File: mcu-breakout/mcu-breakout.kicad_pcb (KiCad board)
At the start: 2 copper layers, 47 x 59.5 mm, 21 parts, among them J1 SCALE 3, J2 SCALE 2, J3 SCALE 1, J4 Spare, J5 Environment, SW1 Mod, SW2 Reset

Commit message: initial version for production
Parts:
- added REF**: Mounting Hole, Chof747_BoardModifications:Mounting Hole, F.Cu at (78.0, 54.9)
- added REF**: Mounting Hole, Chof747_BoardModifications:Mounting Hole, F.Cu at (117.8, 107.2)
- J5: footprint Connector_JST:JST_XH_B4B-XH-A_1x04_P2.50mm_Vertical -> Chof747_Connectors:JST_XH_B4B-XH-A_1x04_P2.54mm_Vertical
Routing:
- net AREF: track 124.2 -> 119.6 mm
- net LED_2: track 97.9 -> 97.1 mm
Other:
- outline, holes or cut-outs redrawn
- board text added: "5V"
- board text removed: "VCC (5V)"

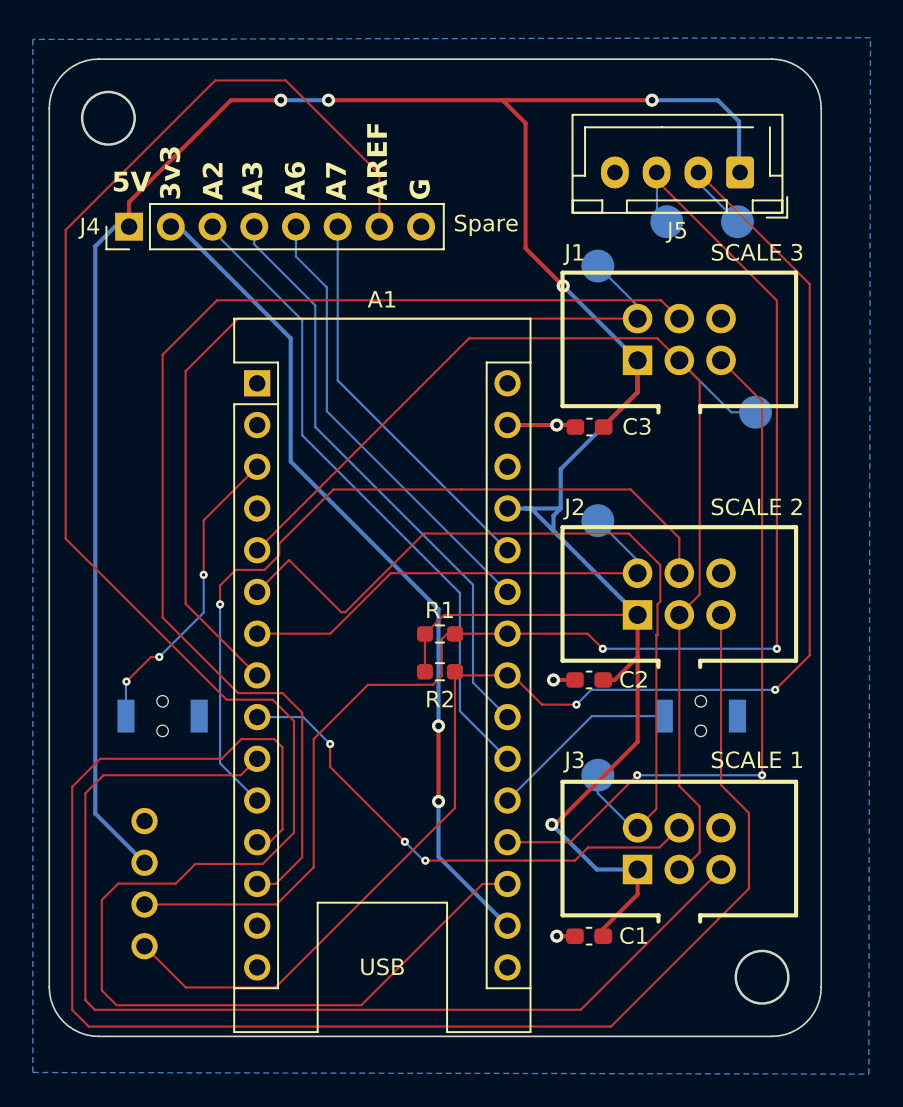
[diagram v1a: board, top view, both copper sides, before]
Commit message: Changed to separeted clock lines for the different scales
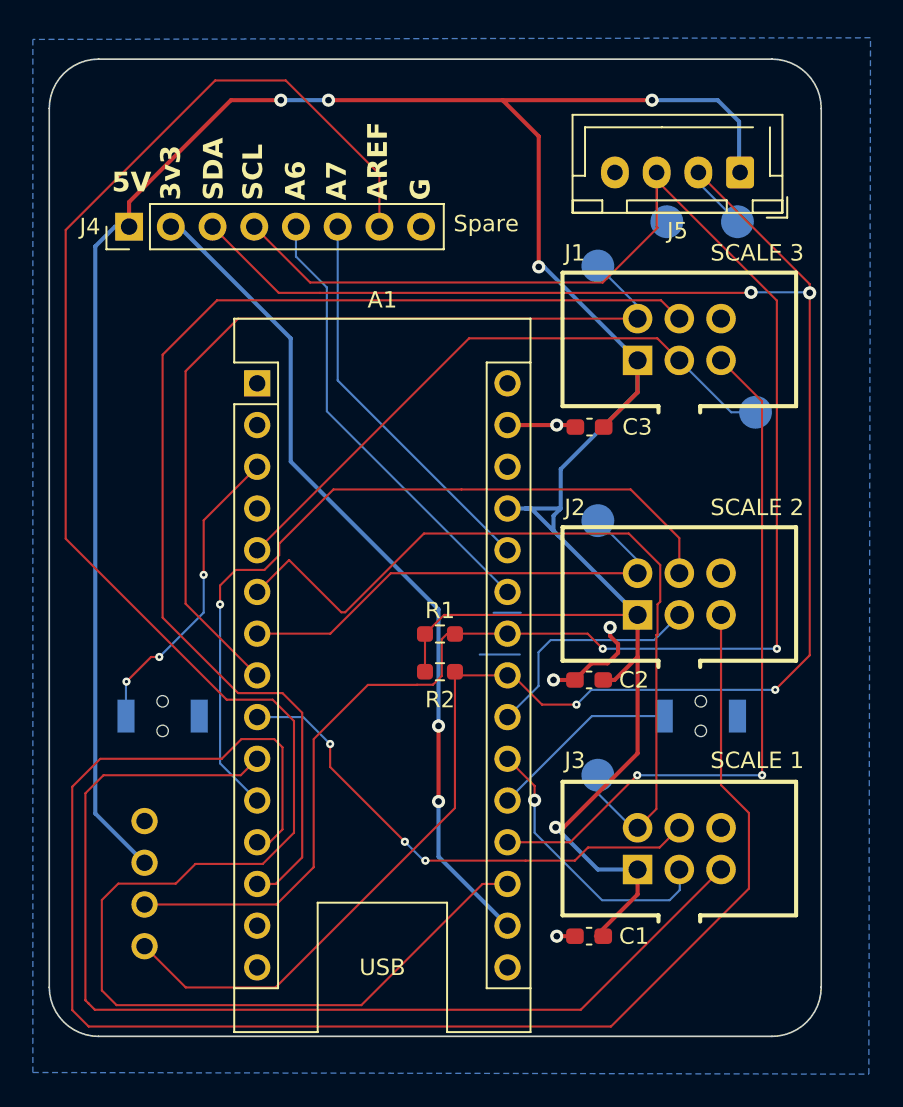
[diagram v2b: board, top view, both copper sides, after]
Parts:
- removed REF** (x2): Mounting Hole, Chof747_BoardModifications:Mounting Hole
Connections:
- A1 pad 21: A2 -> CLK_1
- A1 pad 22: A3 -> CLK_2
- A1 pad 5: CLK -> CLK_3
- J1 pad 3: CLK -> CLK_3
- J2 pad 3: CLK -> CLK_2
- J3 pad 3: CLK -> CLK_1
- J4 pad 3: A2 -> SDA
- J4 pad 4: A3 -> SCL
- TP4 pad 1: CLK -> CLK_3
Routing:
- net CLK: track 70.7 -> 0.00 mm
- net A2: track 39.8 -> 0.00 mm
- net SDA: track 92.6 -> 130.7 mm, vias 2 -> 4
- net CLK_3: track 0.00 -> 37.5 mm
- net A3: track 36.2 -> 0.00 mm
- net SCL: track 86.9 -> 117.6 mm
- net CLK_1: track 0.00 -> 17.2 mm, vias 0 -> 1
- net CLK_2: track 0.00 -> 14.2 mm
- net GND: track 6.59 -> 15.7 mm, vias 3 -> 4
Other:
- board text added: "Samla Filamentalist Controller Board v1.1 (c)2026 chof"
- board text removed: "A2"
- board text removed: "A3"
- board text removed: "Samla Filamentalist Controller Board v1.0 (c)2025 chof"

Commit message: changed to pico as a mcu
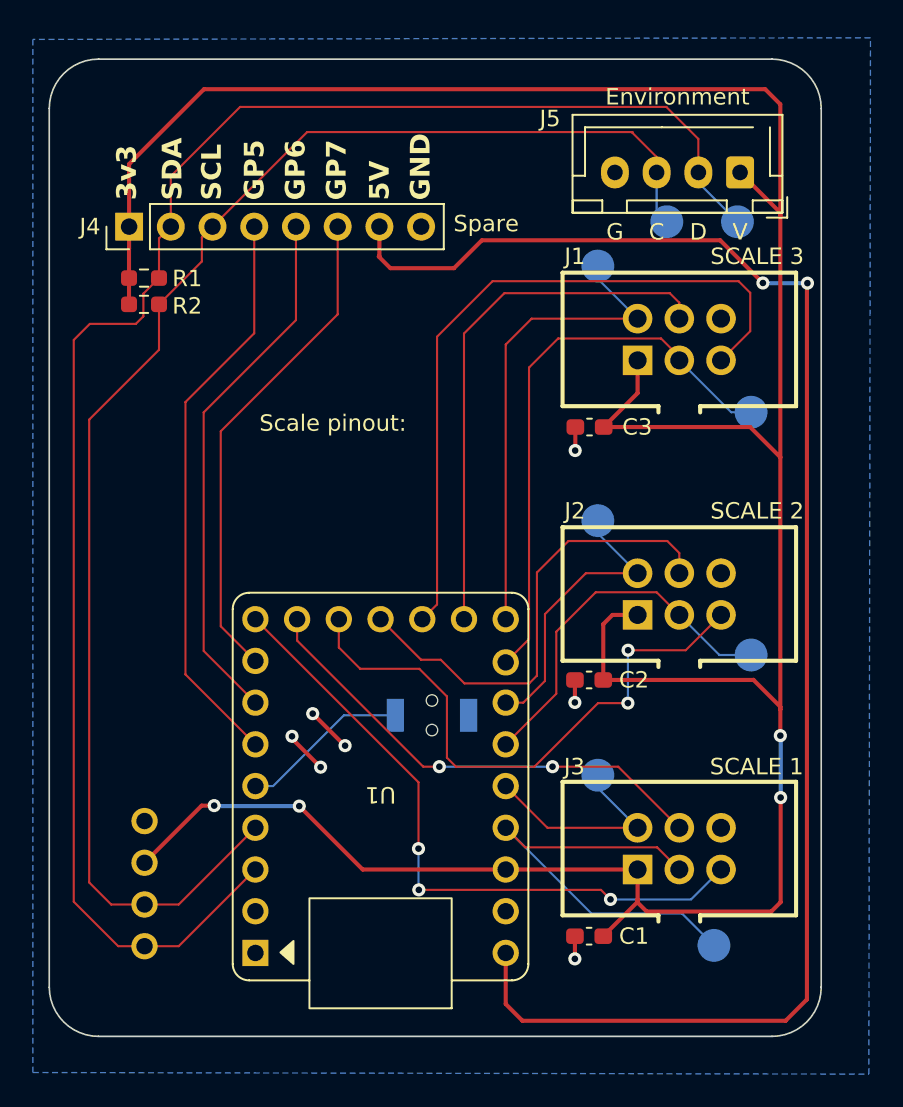
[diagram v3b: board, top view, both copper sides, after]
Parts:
- removed A1: Arduino_Nano_v3.x, Module:Arduino_Nano
- removed SW2: Reset, Chof747_Footprints:KEY-SMD_L3.9-W3.0-LS5.0-EH
- added TP7: Clk 2, TestPoint:TestPoint_Pad_D2.0mm, B.Cu at (117.1, 87.6)
- added TP8: Clk 1, TestPoint:TestPoint_Pad_D2.0mm, B.Cu at (114.9, 105.3)
- added U1: RP2040-ZERO, Chof747_MCUs:RP2040-ZERO-THP, F.Cu at (94.6, 95.6)
- TP4: value Clk -> Clk 3
- moved R2 30.0 mm to (80.2, 64.6)
- moved R1 27.0 mm to (80.2, 66.2)
- moved SW1 16.4 mm to (97.7, 91.2)
- moved TP4 0.27 mm to (117.1, 72.8)
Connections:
- J4 pad 2: +3V3 -> SDA
- J4 pad 3: SDA -> SCL
- J4 pad 4: SCL -> GP5
- J4 pad 5: A6 -> GP6
- J4 pad 6: A7 -> GP7
- J4 pad 7: AREF -> +5V
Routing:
- net AREF: track 119.6 -> 0.00 mm
- net +5V: track 0.00 -> 96.0 mm, vias 0 -> 2
- net LED_2: track 97.1 -> 35.9 mm, vias 0 -> 2
- net +3V3: track 51.3 -> 0.00 mm, vias 2 -> 0
- net BTN_3: track 72.4 -> 32.7 mm
- net DAT_1: track 50.4 -> 13.3 mm
- net GP5: track 0.00 -> 35.3 mm
- net GP6: track 0.00 -> 32.6 mm
- net GP7: track 0.00 -> 30.3 mm
- net SCL: track 117.6 -> 89.7 mm, vias 2 -> 0
- net A6: track 27.6 -> 0.00 mm
- net SDA: track 130.7 -> 103.3 mm, vias 4 -> 0
- net LED_1: track 66.4 -> 40.0 mm, vias 0 -> 3
- net A7: track 24.0 -> 0.00 mm
- net DAT_3: track 53.4 -> 29.6 mm
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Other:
- board text added: "C"
- board text added: "D"
- board text added: "GND"
- board text added: "GP5"
- board text added: "GP6"
- board text added: "GP7"
- board text added: "Samla Filamentalist Controller Board v1.1/Pico (c)2026 chof"
- board text added: "Scale pinout:"
- board text added: "V"
- board text removed: "A6"
- board text removed: "A7"
- board text removed: "AREF"
- board text removed: "Samla Filamentalist Controller Board v1.1 (c)2026 chof"
